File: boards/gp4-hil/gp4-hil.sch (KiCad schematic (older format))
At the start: 0 parts

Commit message: Continued work on gp4-hil board schematic
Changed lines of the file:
@@
 Sheet 1 7
 Title "GreenPak Hardware-In-Loop Test Platform"
-Date "2016-05-09"
+Date "2016-05-10"
 Rev "0.1"
 Comp "Andrew Zonenberg"
@@
 F0 "Power supply" 60
 F1 "psu.sch" 60
+F2 "DUT_VPP" O R 2550 1350 60
+F3 "2V5" O R 2550 1750 60
+F4 "1V8" O R 2550 1850 60
+F5 "1V2" O R 2550 1950 60
+F6 "1V0" O R 2550 2050 60
+F7 "GND" O R 2550 2250 60
+F8 "DUT_VDD1" O R 2550 1450 60
+F9 "DUT_VDD2" O R 2550 1550 60
 $EndSheet
 $Sheet
@@
 F0 "DUT" 60
 F1 "dut.sch" 60
+F2 "DUT_VDD1" I L 6600 1450 60
+F3 "DUT_VPP" I L 6600 1350 60
+F4 "DUT_VDD2" I L 6600 1550 60
+F5 "GND" I L 6600 2250 60
 $EndSheet
 $Sheet

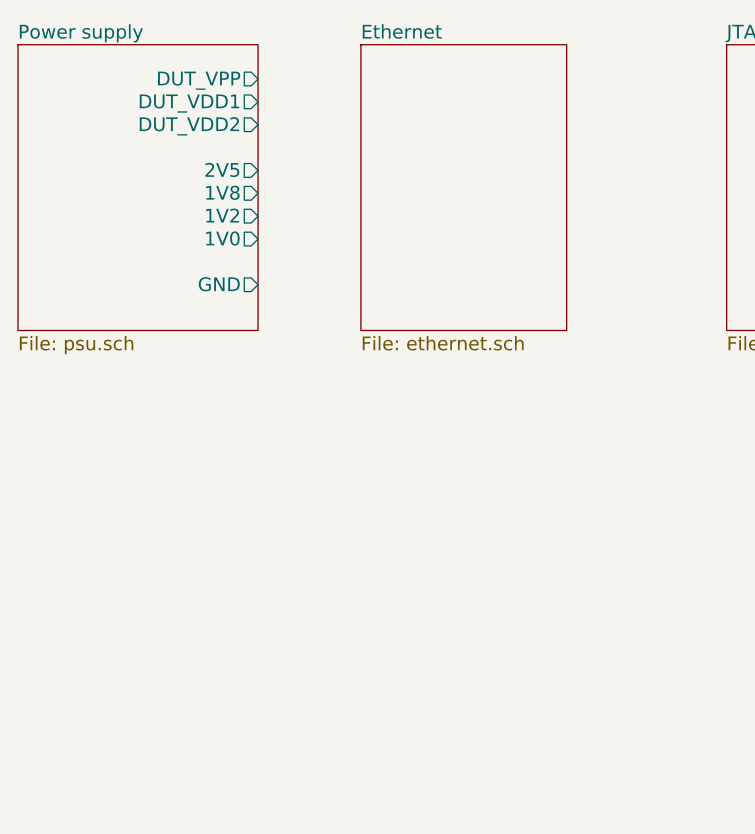
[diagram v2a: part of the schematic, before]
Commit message: Began schematic capture for Ethernet on test board
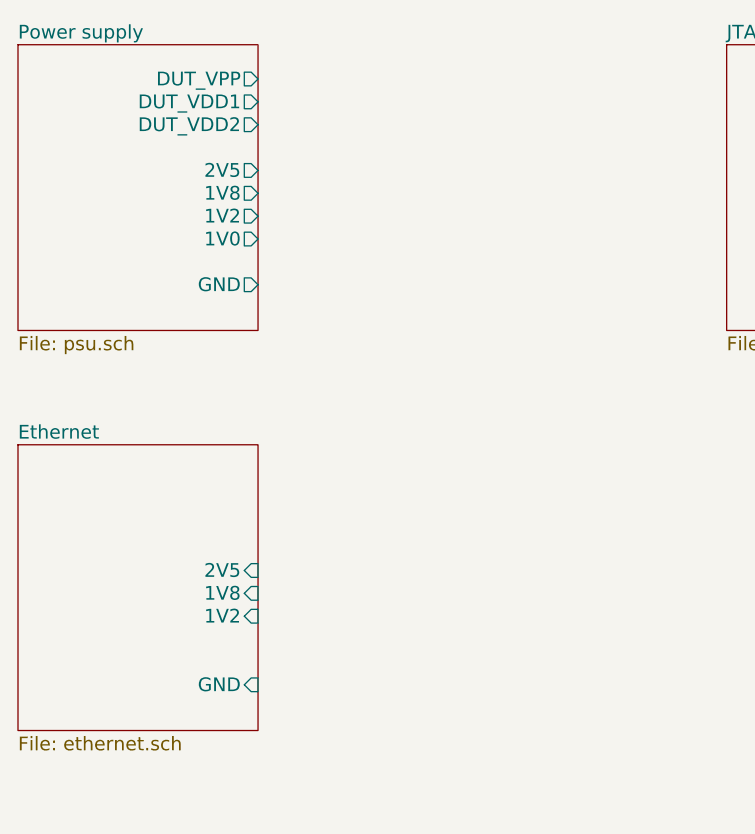
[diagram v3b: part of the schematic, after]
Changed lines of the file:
@@
 LIBS:xilinx-azonenberg
 LIBS:conn
+LIBS:device
 LIBS:gp4-hil-cache
 EELAYER 25 0
@@
 Sheet 1 7
 Title "GreenPak Hardware-In-Loop Test Platform"
-Date "2016-05-10"
+Date "2016-05-11"
 Rev "0.1"
 Comp "Andrew Zonenberg"
@@
 $EndSheet
 $Sheet
-S 3000 1200 900  1250
+S 1500 2950 1050 1250
 U 57316A40
 F0 "Ethernet" 60
 F1 "ethernet.sch" 60
+F2 "2V5" I R 2550 3500 60
+F3 "1V8" I R 2550 3600 60
+F4 "1V2" I R 2550 3700 60
+F5 "GND" I R 2550 4000 60
 $EndSheet
 $Sheet

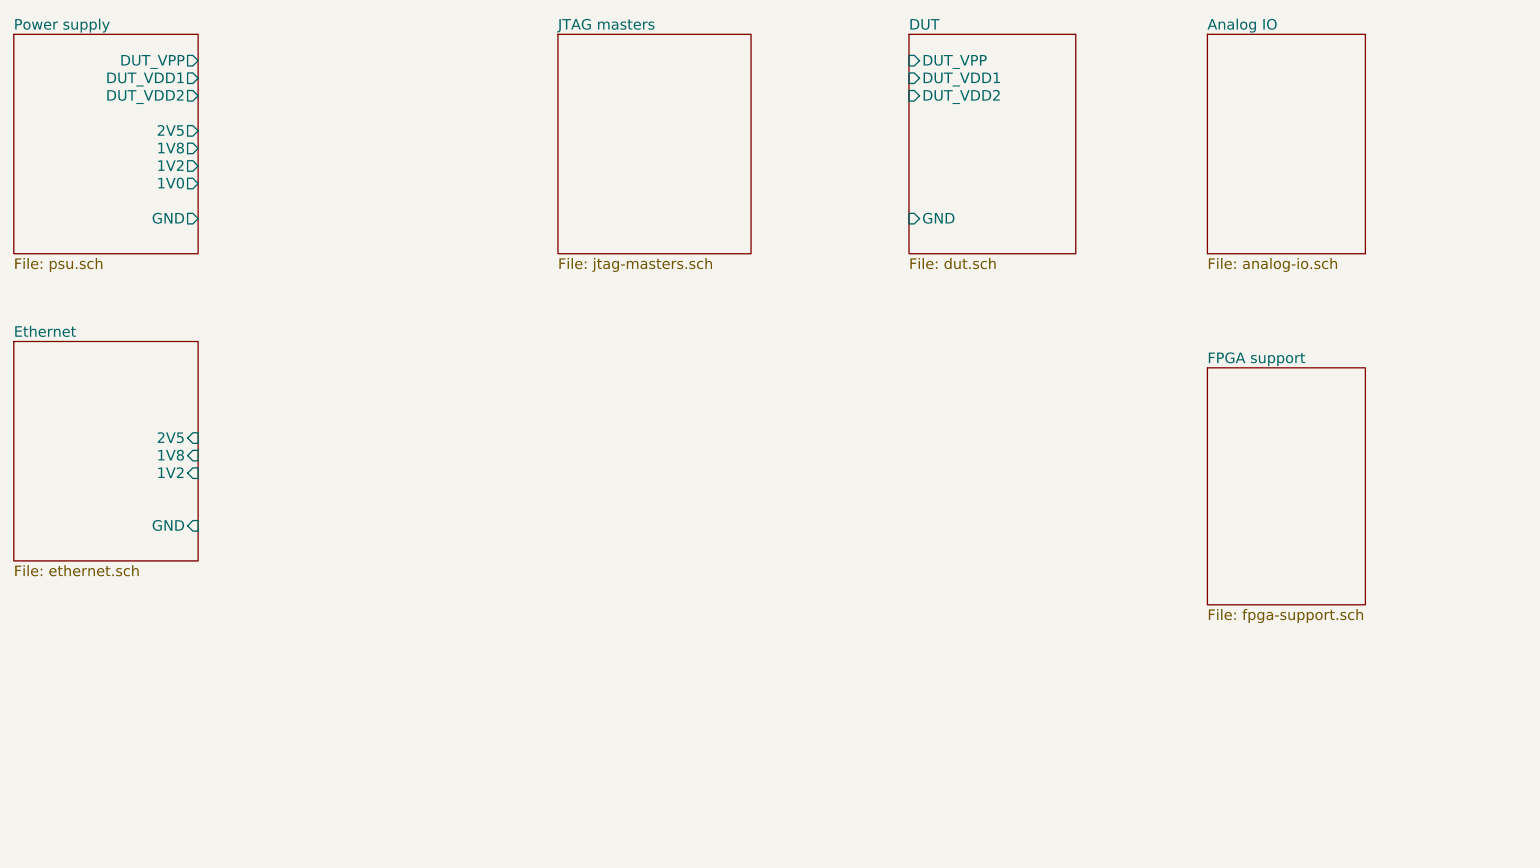
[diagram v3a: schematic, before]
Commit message: Continued analog input schematic
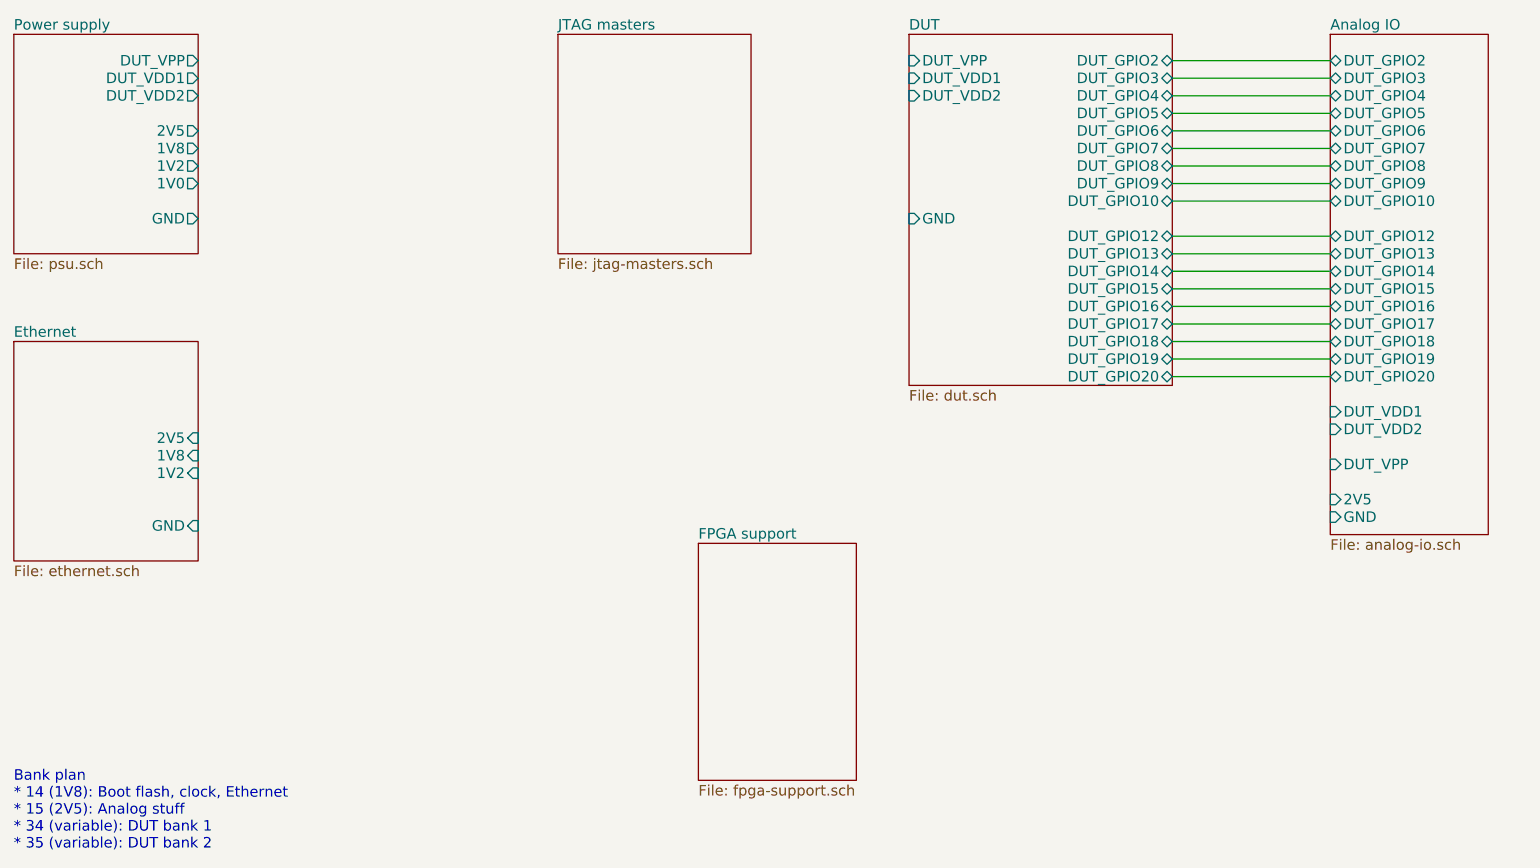
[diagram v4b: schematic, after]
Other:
- note added: "Bank plan\n* 14 (1V8): Boot flash, clock, Ethernet\n* 15 (2V5): Analog stuff\n* 34 (variable): DUT bank 1\n* 35 (variable): DUT bank 2"
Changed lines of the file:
@@
 $EndSheet
 $Sheet
-S 6600 1200 950  1250
+S 6600 1200 1500 2000
 U 57316A58
 F0 "DUT" 60
@@
 F4 "DUT_VDD2" I L 6600 1550 60
 F5 "GND" I L 6600 2250 60
+F6 "DUT_GPIO2" B R 8100 1350 60
+F7 "DUT_GPIO3" B R 8100 1450 60
+F8 "DUT_GPIO4" B R 8100 1550 60
+F9 "DUT_GPIO5" B R 8100 1650 60
+F10 "DUT_GPIO6" B R 8100 1750 60
+F11 "DUT_GPIO7" B R 8100 1850 60
+F12 "DUT_GPIO8" B R 8100 1950 60
+F13 "DUT_GPIO9" B R 8100 2050 60
+F14 "DUT_GPIO10" B R 8100 2150 60
+F15 "DUT_GPIO12" B R 8100 2350 60
+F16 "DUT_GPIO13" B R 8100 2450 60
+F17 "DUT_GPIO14" B R 8100 2550 60
+F18 "DUT_GPIO15" B R 8100 2650 60
+F19 "DUT_GPIO16" B R 8100 2750 60
+F20 "DUT_GPIO17" B R 8100 2850 60
+F21 "DUT_GPIO18" B R 8100 2950 60
+F22 "DUT_GPIO19" B R 8100 3050 60
+F23 "DUT_GPIO20" B R 8100 3150 60
 $EndSheet
 $Sheet
-S 8300 1200 900  1250
+S 9000 1200 900  2850
 U 57316A68
 F0 "Analog IO" 60
 F1 "analog-io.sch" 60
+F2 "DUT_VDD1" I L 9000 3350 60
+F3 "DUT_VDD2" I L 9000 3450 60
+F4 "GND" I L 9000 3950 60
+F5 "DUT_VPP" I L 9000 3650 60
+F6 "DUT_GPIO2" B L 9000 1350 60
+F7 "DUT_GPIO3" B L 9000 1450 60
+F8 "DUT_GPIO4" B L 9000 1550 60
+F9 "DUT_GPIO5" B L 9000 1650 60
+F10 "DUT_GPIO6" B L 9000 1750 60
+F11 "DUT_GPIO7" B L 9000 1850 60
+F12 "DUT_GPIO8" B L 9000 1950 60
+F13 "DUT_GPIO9" B L 9000 2050 60
+F14 "DUT_GPIO10" B L 9000 2150 60
+F15 "DUT_GPIO12" B L 9000 2350 60
+F16 "DUT_GPIO13" B L 9000 2450 60
+F17 "DUT_GPIO14" B L 9000 2550 60
+F18 "DUT_GPIO15" B L 9000 2650 60
+F19 "DUT_GPIO16" B L 9000 2750 60
+F20 "DUT_GPIO17" B L 9000 2850 60
+F21 "DUT_GPIO18" B L 9000 2950 60
+F22 "DUT_GPIO19" B L 9000 3050 60
+F23 "DUT_GPIO20" B L 9000 3150 60
+F24 "2V5" I L 9000 3850 60
 $EndSheet
 $Sheet
-S 8300 3100 900  1350
+S 5400 4100 900  1350
 U 57316B0C
 F0 "FPGA support" 60
 F1 "fpga-support.sch" 60
 $EndSheet
+Text Notes 1500 5850 0    60   ~ 0
+Bank plan\n* 14 (1V8): Boot flash, clock, Ethernet\n* 15 (2V5): Analog stuff\n* 34 (variable): DUT bank 1\n* 35 (variable): DUT bank 2
+Wire Wire Line
+	8100 1350 9000 1350
+Wire Wire Line
+	9000 1450 8100 1450
+Wire Wire Line
+	8100 1550 9000 1550
+Wire Wire Line
+	9000 1650 8100 1650
+Wire Wire Line
+	8100 1750 9000 1750
+Wire Wire Line
+	9000 1850 8100 1850
+Wire Wire Line
+	8100 1950 9000 1950
+Wire Wire Line
+	9000 2050 8100 2050
+Wire Wire Line
+	8100 2150 9000 2150
+Wire Wire Line
+	9000 2350 8100 2350
+Wire Wire Line
+	8100 2450 9000 2450
+Wire Wire Line
+	9000 2550 8100 2550
+Wire Wire Line
+	8100 2650 9000 2650
+Wire Wire Line
+	9000 2750 8100 2750
+Wire Wire Line
+	8100 2850 9000 2850
+Wire Wire Line
+	9000 2950 8100 2950
+Wire Wire Line
+	8100 3050 9000 3050
+Wire Wire Line
+	9000 3150 8100 3150
 $EndSCHEMATC

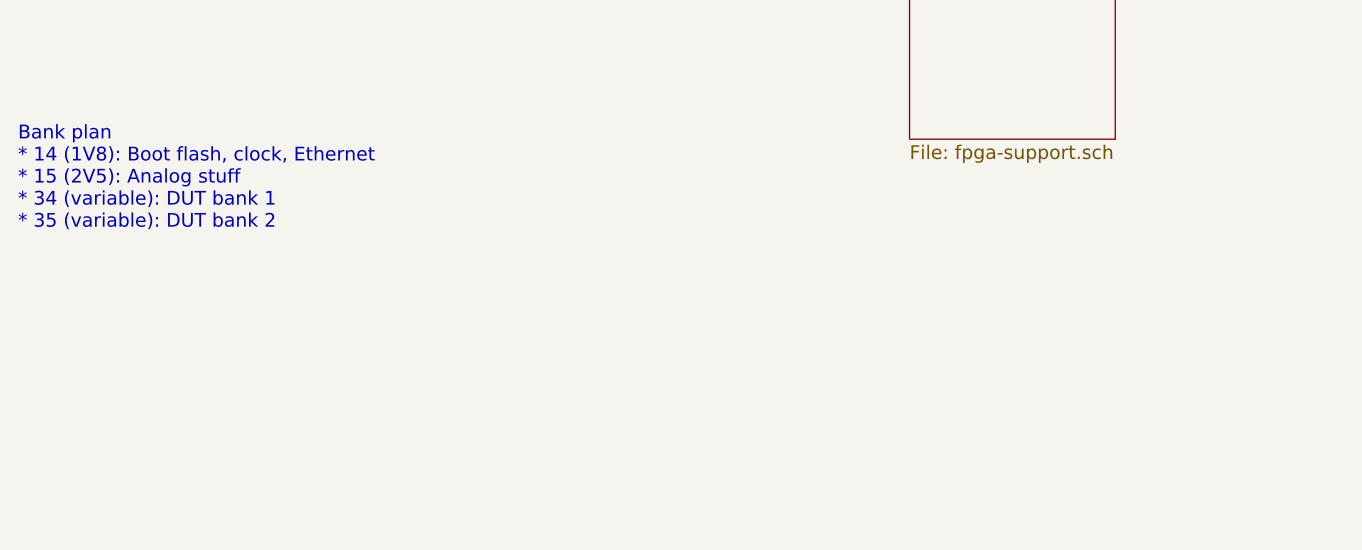
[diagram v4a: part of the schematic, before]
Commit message: Continued ADC schematic capture
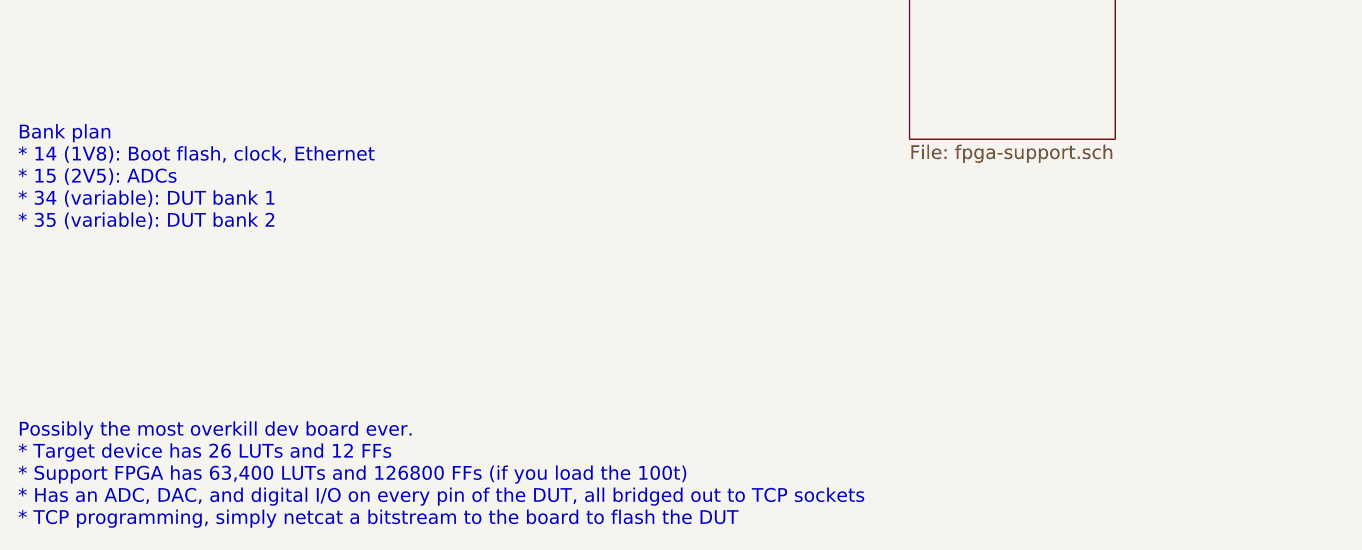
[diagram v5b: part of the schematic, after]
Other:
- note added: "Bank plan\n* 14 (1V8): Boot flash, clock, Ethernet\n* 15 (2V5): ADCs\n* 34 (variable): DUT bank 1\n* 35 (variable): DUT bank 2"
- note added: "Possibly the most overkill dev board ever.\n* Target device has 26 LUTs and 12 FFs\n* Support FPGA has 63,400 LUTs and 126800 FFs (if you load the 100t)\n* Has an ADC, DAC, and digital I/O on every pin of the DUT, all bridged out to TCP sockets\n* TCP programming, simply netcat a bitstream to the board to flash the DUT"
- note removed: "Bank plan\n* 14 (1V8): Boot flash, clock, Ethernet\n* 15 (2V5): Analog stuff\n* 34 (variable): DUT bank 1\n* 35 (variable): DUT bank 2"
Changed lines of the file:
@@
 Sheet 1 7
 Title "GreenPak Hardware-In-Loop Test Platform"
-Date "2016-05-11"
+Date "2016-05-12"
 Rev "0.1"
 Comp "Andrew Zonenberg"
@@
 $EndSheet
 Text Notes 1500 5850 0    60   ~ 0
-Bank plan\n* 14 (1V8): Boot flash, clock, Ethernet\n* 15 (2V5): Analog stuff\n* 34 (variable): DUT bank 1\n* 35 (variable): DUT bank 2
+Bank plan\n* 14 (1V8): Boot flash, clock, Ethernet\n* 15 (2V5): ADCs\n* 34 (variable): DUT bank 1\n* 35 (variable): DUT bank 2
 Wire Wire Line
 	8100 1350 9000 1350
@@
 Wire Wire Line
 	9000 3150 8100 3150
+Text Notes 1500 7150 0    60   ~ 0
+Possibly the most overkill dev board ever.\n* Target device has 26 LUTs and 12 FFs\n* Support FPGA has 63,400 LUTs and 126800 FFs (if you load the 100t)\n* Has an ADC, DAC, and digital I/O on every pin of the DUT, all bridged out to TCP sockets\n* TCP programming, simply netcat a bitstream to the board to flash the DUT
 $EndSCHEMATC

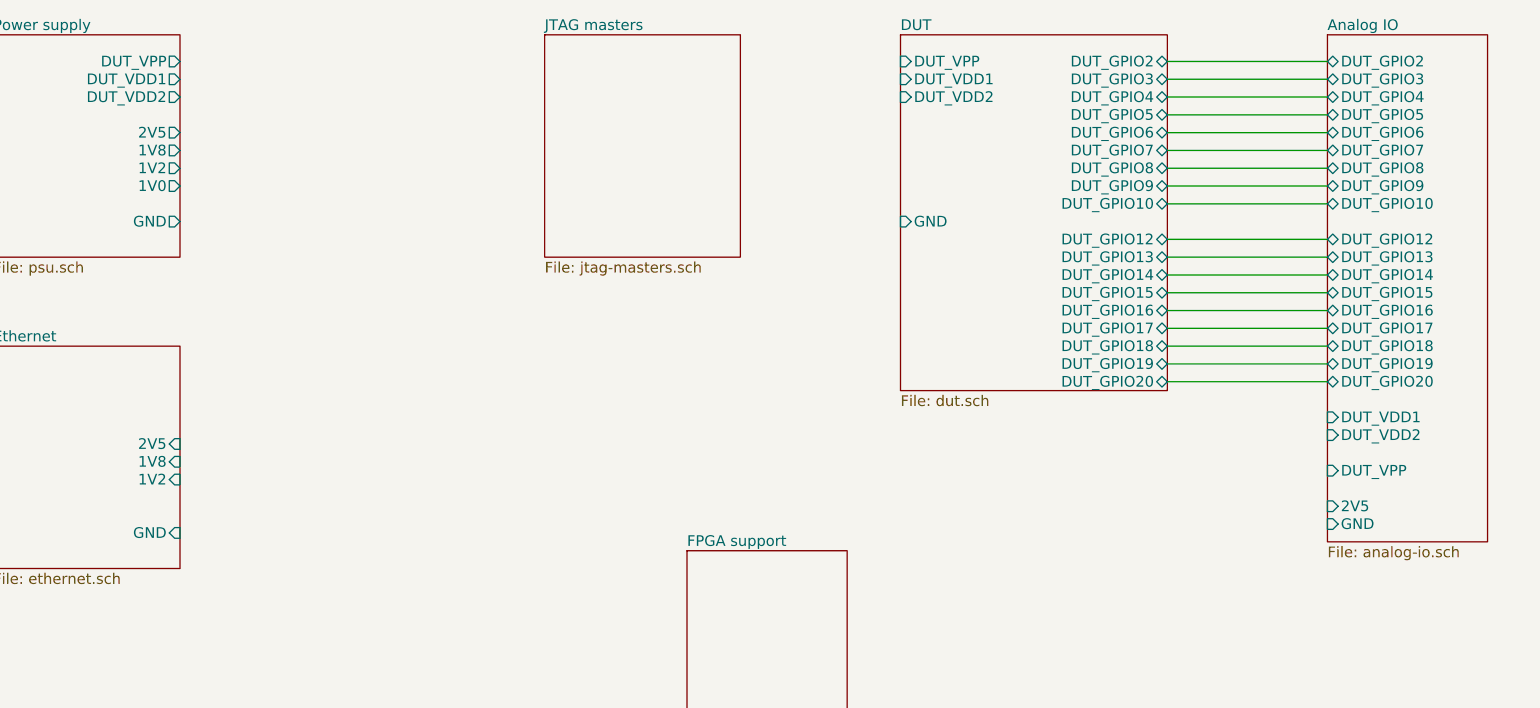
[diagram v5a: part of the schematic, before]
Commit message: Added DACs, minor page layout tweaks, lots of decoupling
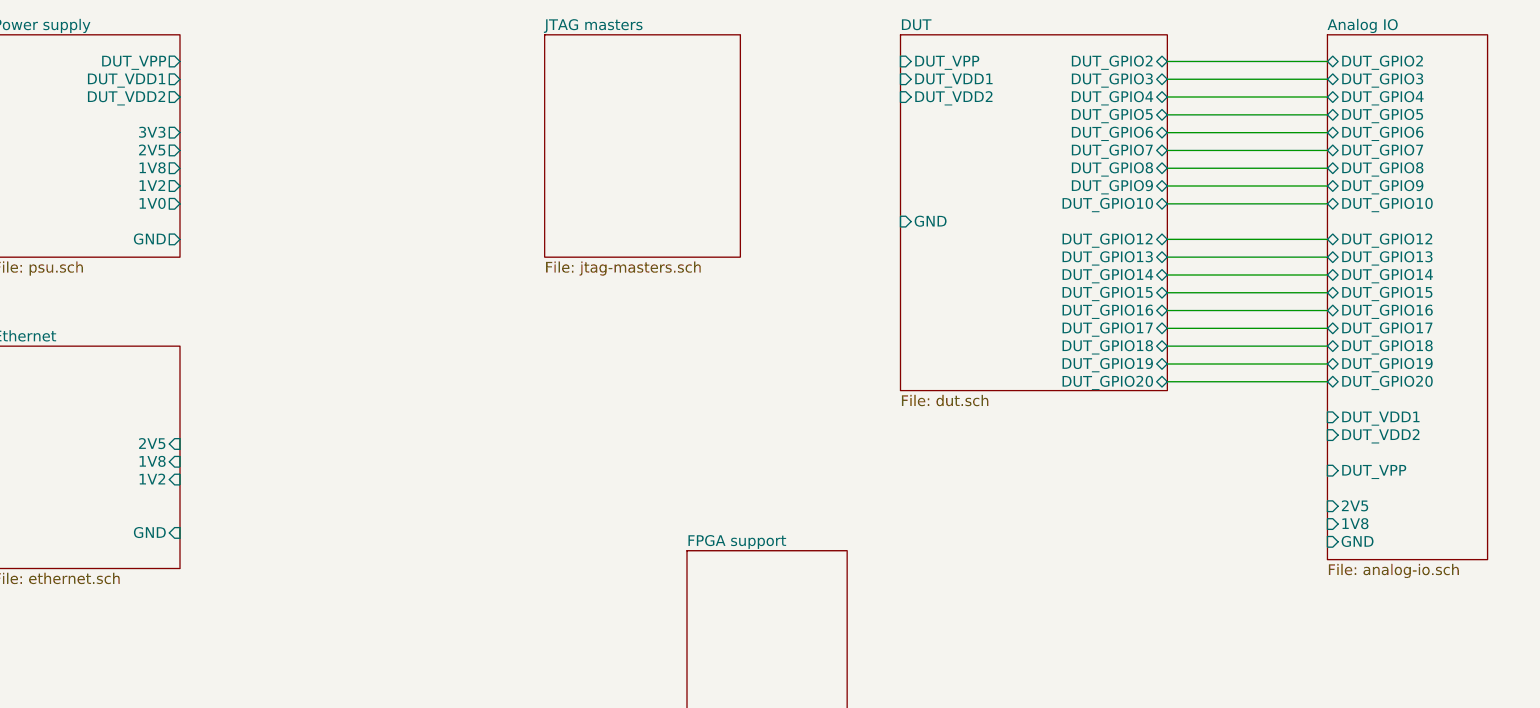
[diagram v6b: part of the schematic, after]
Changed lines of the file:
@@
 EELAYER 25 0
 EELAYER END
-$Descr A4 11693 8268
+$Descr A2 23386 16535
 encoding utf-8
 Sheet 1 7
 Title "GreenPak Hardware-In-Loop Test Platform"
-Date "2016-05-12"
+Date "2016-05-13"
 Rev "0.1"
 Comp "Andrew Zonenberg"
@@
 F1 "psu.sch" 60
 F2 "DUT_VPP" O R 2550 1350 60
-F3 "2V5" O R 2550 1750 60
-F4 "1V8" O R 2550 1850 60
-F5 "1V2" O R 2550 1950 60
-F6 "1V0" O R 2550 2050 60
-F7 "GND" O R 2550 2250 60
+F3 "2V5" O R 2550 1850 60
+F4 "1V8" O R 2550 1950 60
+F5 "1V2" O R 2550 2050 60
+F6 "1V0" O R 2550 2150 60
+F7 "GND" O R 2550 2350 60
 F8 "DUT_VDD1" O R 2550 1450 60
 F9 "DUT_VDD2" O R 2550 1550 60
+F10 "3V3" O R 2550 1750 60
 $EndSheet
 $Sheet
@@
 $EndSheet
 $Sheet
-S 9000 1200 900  2850
+S 9000 1200 900  2950
 U 57316A68
 F0 "Analog IO" 60
@@
 F2 "DUT_VDD1" I L 9000 3350 60
 F3 "DUT_VDD2" I L 9000 3450 60
-F4 "GND" I L 9000 3950 60
+F4 "GND" I L 9000 4050 60
 F5 "DUT_VPP" I L 9000 3650 60
 F6 "DUT_GPIO2" B L 9000 1350 60
@@
 F23 "DUT_GPIO20" B L 9000 3150 60
 F24 "2V5" I L 9000 3850 60
+F25 "1V8" I L 9000 3950 60
 $EndSheet
 $Sheet
